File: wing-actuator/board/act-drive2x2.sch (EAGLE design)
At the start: 104 parts, among them J1 POWER_JACKPTH_LOCK, Q1 BSS123, Q2 BSS123, U5 Q50-5C, U7 LP2985-33, U8 TPS62160, X1 SMA-142-0701-801/806, X2 SMA-142-0701-801/806, X3 SMA-142-0701-801/806, X4 SMA-142-0701-801/806, X5 2516-

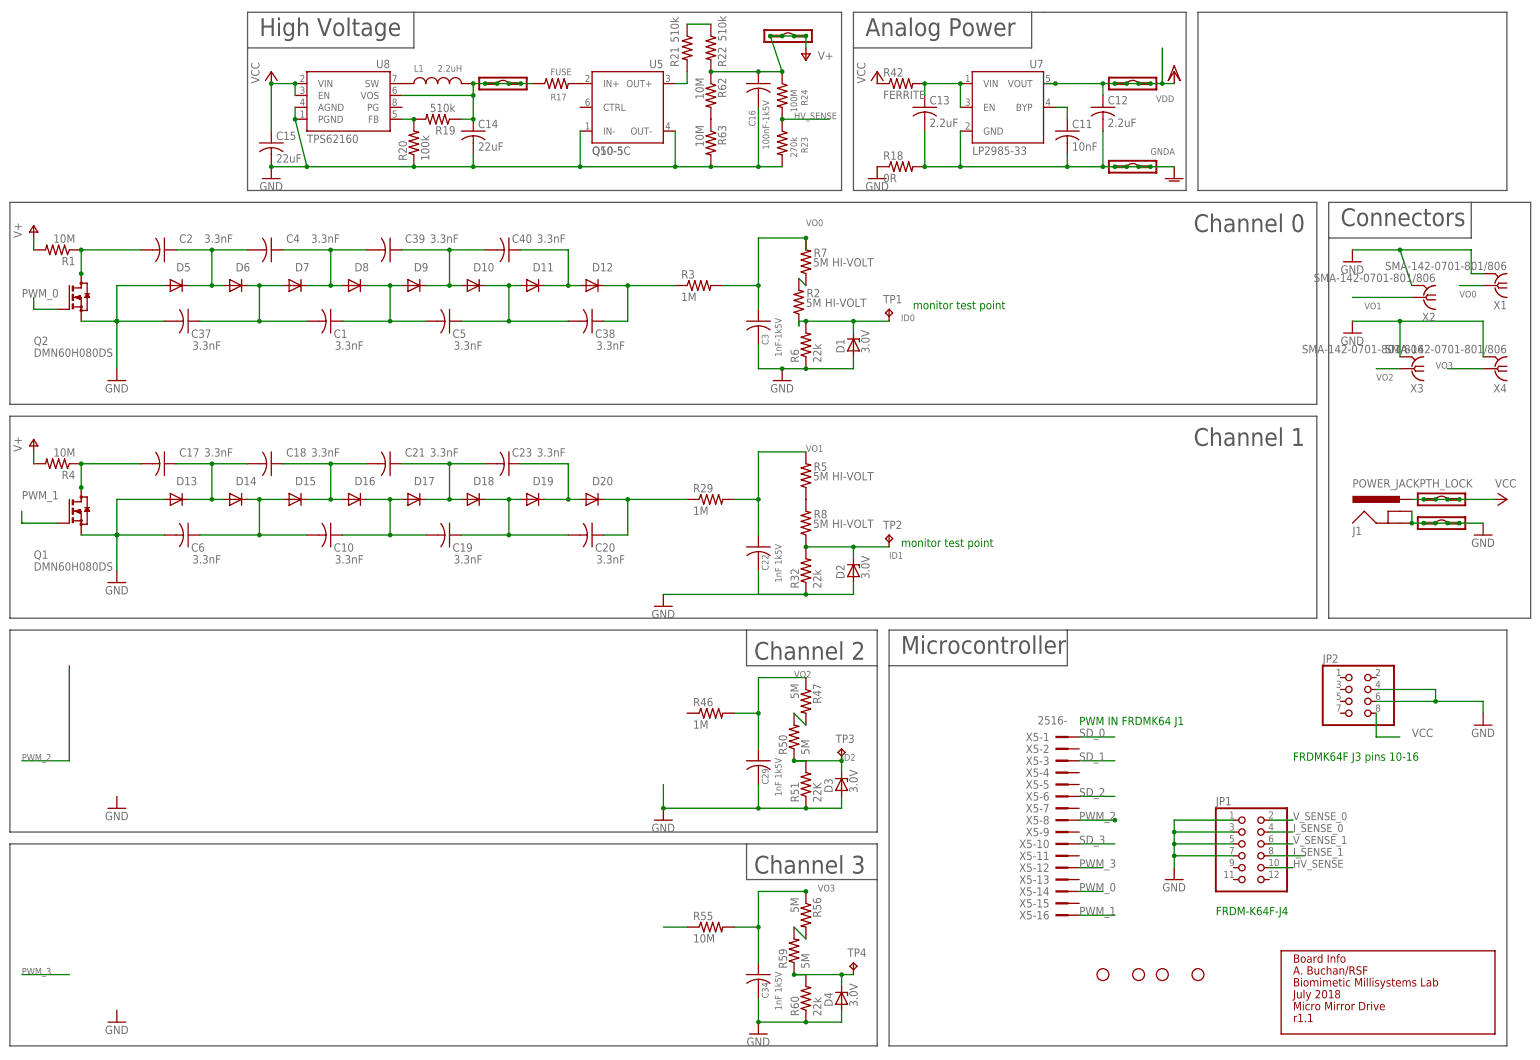
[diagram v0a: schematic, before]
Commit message: adding 2x2 array
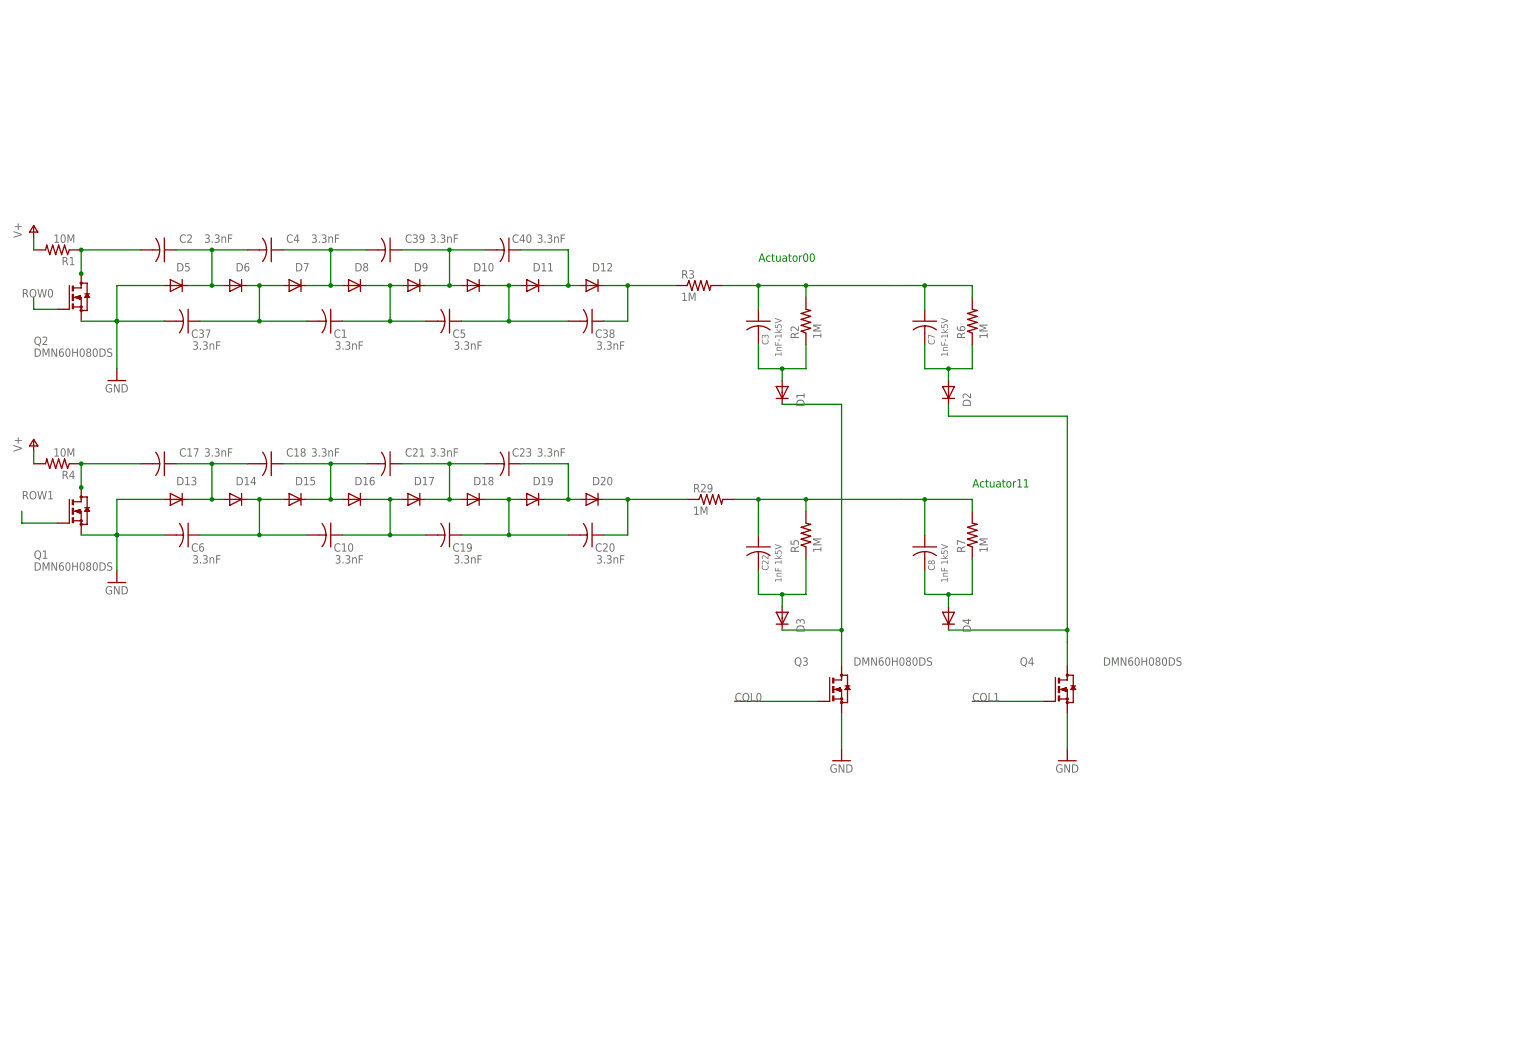
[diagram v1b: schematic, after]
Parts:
- removed C11: 10nF, rcl:C-USC1206
- removed C12, C13: 2.2uF, rcl:C-USC1206
- removed C14, C15: 22uF, rcl:C-USC1206
- removed C16: 100nF-1k5V, rcl:C-USC2225K
- removed C29, C34: 1nF 1k5V, rcl:C-USC1206
- removed GND, GNDA, HV_IN, HV_OUT, VCC, VDDA: (no value), modular_robotics:M04LOCK
- removed H5, H6, H7, H8: STAND-OFFTIGHT, SparkFun-Hardware:STAND-OFFTIGHT
- removed J1: POWER_JACKPTH_LOCK, SparkFun-Connectors:POWER_JACKPTH_LOCK
- removed JP1: (no value), pinhead:PINHD-2X6
- removed JP2: (no value), pinhead:PINHD-2X4
- removed L1: 2.2uH, modular_robotics:INDUCTOR
- removed R17: FUSE, rcl:R-US_R1206
- removed R18: 0R, rcl:R-US_R1206
- removed R19, R21, R22: 510k, rcl:R-US_R1206
- removed R20: 100k, rcl:R-US_R1206
- removed R23: 270k, rcl:R-US_R1206
- removed R24: 100M, rcl:R-US_R1206
- removed R32, R60: 22k, rcl:R-US_R1206
- removed R42: FERRITE, rcl:R-US_R1206
- removed R46: 1M, rcl:R-US_R1206
- removed R47, R50, R56, R59, R8: 5M, rcl:R-US_R1206
- removed R51: 22K, rcl:R-US_R1206
- removed R55, R62, R63: 10M, rcl:R-US_R1206
- removed TP1, TP2, TP3, TP4: TPTP10SQ, testpad:TPTP10SQ
- removed U$18: INFO, modular_robotics:INFO
- removed U5: Q50-5C, modular_robotics:Q50-5C
- removed U7: LP2985-33, modular_robotics:LP2985-33
- removed U8: TPS62160, modular_robotics:TPS62160
- removed X1, X2, X3, X4: SMA-142-0701-801/806, con-coax:SMA-142-0701-801/806
- removed X5: 2516-, con-3m:2516-
- added C7: 1nF-1k5V, rcl:C-USC1206
- added C8: 1nF 1k5V, rcl:C-USC1206
- added Q3, Q4: BSS123, transistor-small-signal:BSS123
- D1, D2, D3, D4: value 3.0V -> (none); device diode:ZENER-DIODESOD80C -> diode:DIODE-SOD323-W; PANASONIC (none) -> DA2JF8100L
- R2, R5, R7: value 5M -> 1M; HI-VOLT 800 -> (none)
- R6: value 22k -> 1M
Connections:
- removed net GNDA: C11.2, C12.2, C13.2, GNDA.1, GNDA.2, GNDA.3, GNDA.4, R18.2, U7.GND
- removed net HV_SENSE: JP1.10, R23.1, R24.2
- removed net ID0: D1.C, R2.1, R6.2, TP1.TP
- removed net ID1: D2.C, R32.2, R8.1, TP2.TP
- removed net ID2: D3.C, R50.1, R51.2, TP3.TP
- removed net ID3: D4.C, R59.1, R60.2, TP4.TP
- removed net I_SENSE_0: JP1.4
- removed net I_SENSE_1: JP1.8
- removed net N$20: R19.2, R20.2, U8.FB
- removed net N$24: R21.1, R22.1
- removed net N$25: R47.2, R50.2
- removed net N$26: R55.1
- removed net N$27: R56.2, R59.2
- removed net N$37: C13.1, R42.2, U7.EN, U7.VIN
- removed net N$60: R21.2, U5.OUT+
- removed net N$62: R62.2, R63.1
- removed net PWM_0: Q2.G, X5-14.KL
- removed net PWM_1: Q1.G, X5-16.KL
- removed net PWM_2: X5-8.KL
- removed net PWM_3: X5-12.KL
- removed net SD_0: X5-1.KL
- removed net SD_1: X5-3.KL
- removed net SD_2: X5-6.KL
- removed net SD_3: X5-10.KL
- removed net VCC: C15.1, J1.PWR, JP2.8, R42.1, U8.EN, U8.VIN, VCC.1, VCC.2, VCC.3, VCC.4
- removed net VDDA: C12.1, U7.VOUT, VDDA.1, VDDA.2, VDDA.3, VDDA.4
- removed net VO2: C29.1, R46.2, R47.1, X3.1
- removed net VO3: C34.1, R55.2, R56.1, X4.1
- removed net V_SENSE_0: JP1.2
- removed net V_SENSE_1: JP1.6
- new net COL0: Q3.G
- new net COL1: Q4.G
- new net ROW0: Q2.G
- new net ROW1: Q1.G
- net GND: now also Q3.S, Q4.S; no longer C14.2, C15.2, C16.2, C22.2, C29.2, C3.2, C34.2, D1.A, D2.A, D3.A, D4.A, GND.1, GND.2, GND.3, GND.4, J1.GND, J1.GNDBREAK, JP1.1, JP1.3, JP1.5, JP1.7, JP2.4, JP2.6, R18.1, R20.1, R23.2, R32.1, R51.1, R6.1, R60.1, R63.2, U5.IN-, U5.OUT-, U8.AGND, U8.PGND, X1.2, X2.2, X3.2, X4.2
- net N$12: now also C7.2, D2.A, R6.1; no longer R17.2, U5.IN+
- net N$17: now also C8.2, D4.A, R7.1; no longer L1.1, U8.SW
- net N$18: now also D1.C, D3.C, Q3.D; no longer C14.1, HV_IN.1, HV_IN.2, HV_IN.3, HV_IN.4, L1.2, R17.1, R19.1, U8.VOS
- net N$19: now also D2.C, D4.C, Q4.D; no longer C11.1, U7.BYP
- net N$4: now also C3.2, D1.A, R2.1; no longer R2.2, R7.1
- net N$6: now also C22.2, D3.A; no longer R8.2
- net V+: no longer C16.1, HV_OUT.1, HV_OUT.2, HV_OUT.3, HV_OUT.4, R22.2, R24.1, R62.1
- net VO0: now also C7.1, R2.2, R6.2; no longer R7.2, X1.1
- net VO1: now also C8.1, R7.2; no longer X2.1
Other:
- note added: "Actuator00"
- note added: "Actuator11"
- note removed: "Analog Power"
- note removed: "Channel 0"
- note removed: "Channel 1"
- note removed: "Channel 2"
- note removed: "Channel 3"
- note removed: "Connectors"
- note removed: "FRDM-K64F-J4"
- note removed: "FRDMK64F J3 pins 10-16"
- note removed: "High Voltage"
- note removed: "Microcontroller"
- note removed: "PWM IN FRDMK64 J1"
- note removed: "monitor test point"
- moved on the sheet: R2, R5, R6, R7
